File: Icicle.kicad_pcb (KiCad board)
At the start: 2 copper layers, 216 x 8 mm, 23 parts, among them P1 NeopixelStripPads, P2 NeopixelStripPads

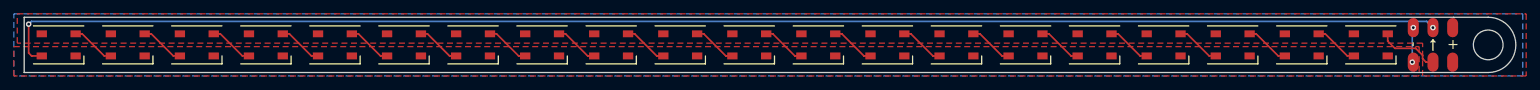
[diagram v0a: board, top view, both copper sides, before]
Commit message: Added a by-pass cap
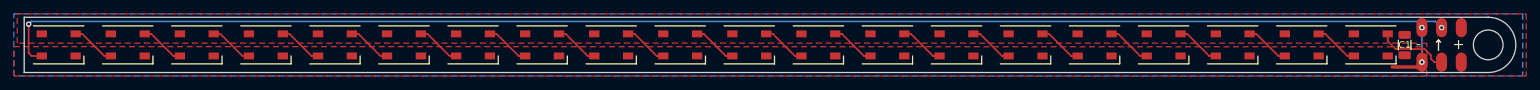
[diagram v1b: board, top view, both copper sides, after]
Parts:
- added C1: 10uF, Capacitor_SMD:C_1206_3216Metric, F.Cu at (229.9, 91.0)
- moved P1 1.25 mm to (235.2, 93.5)
- moved P2 1.25 mm to (235.2, 88.5)
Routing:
- net GND: track 5.30 -> 9.59 mm
- net /DIN: track 9.16 -> 10.4 mm
- net /DOUT: track 210.1 -> 211.4 mm
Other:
- outline, holes or cut-outs redrawn
